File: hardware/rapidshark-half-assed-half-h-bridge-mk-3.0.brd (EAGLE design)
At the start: 25.4 x 40.6 mm, 31 parts, among them Q2 IRF540N

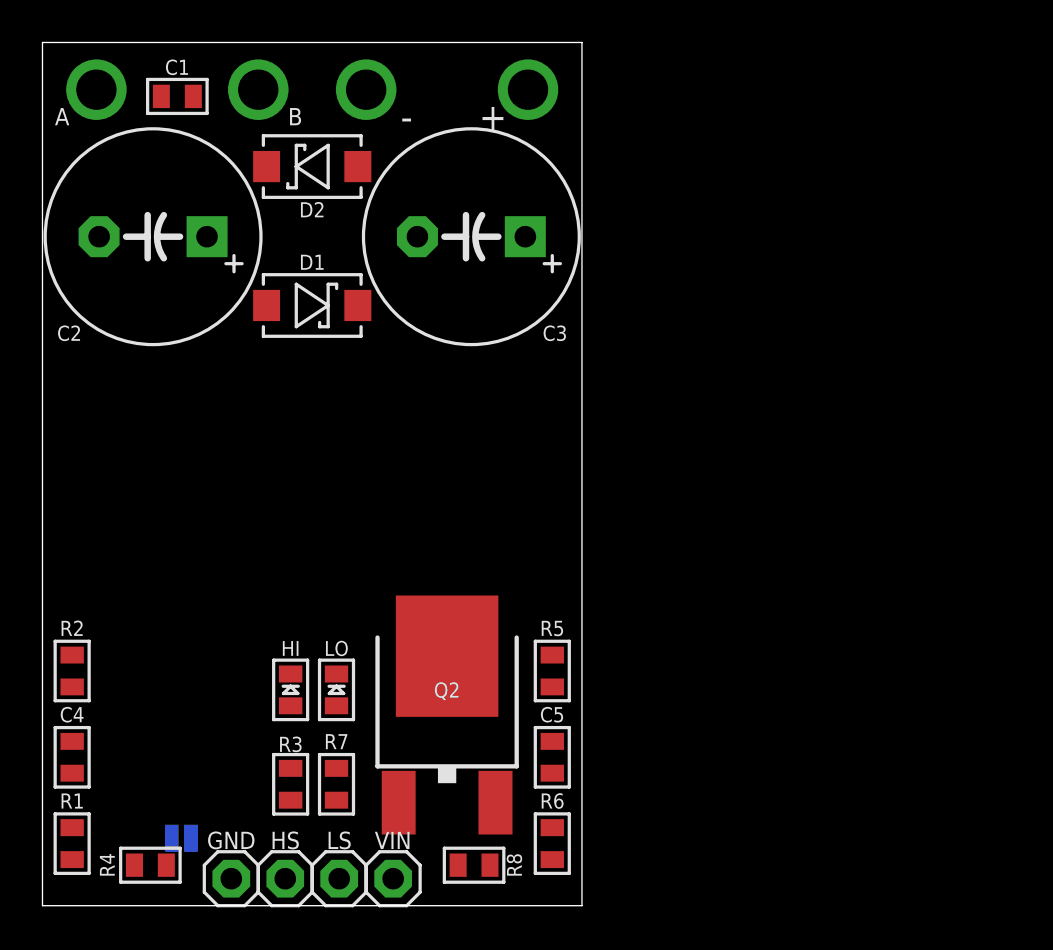
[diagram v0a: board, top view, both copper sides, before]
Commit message: WIP A3946 half bridge driver
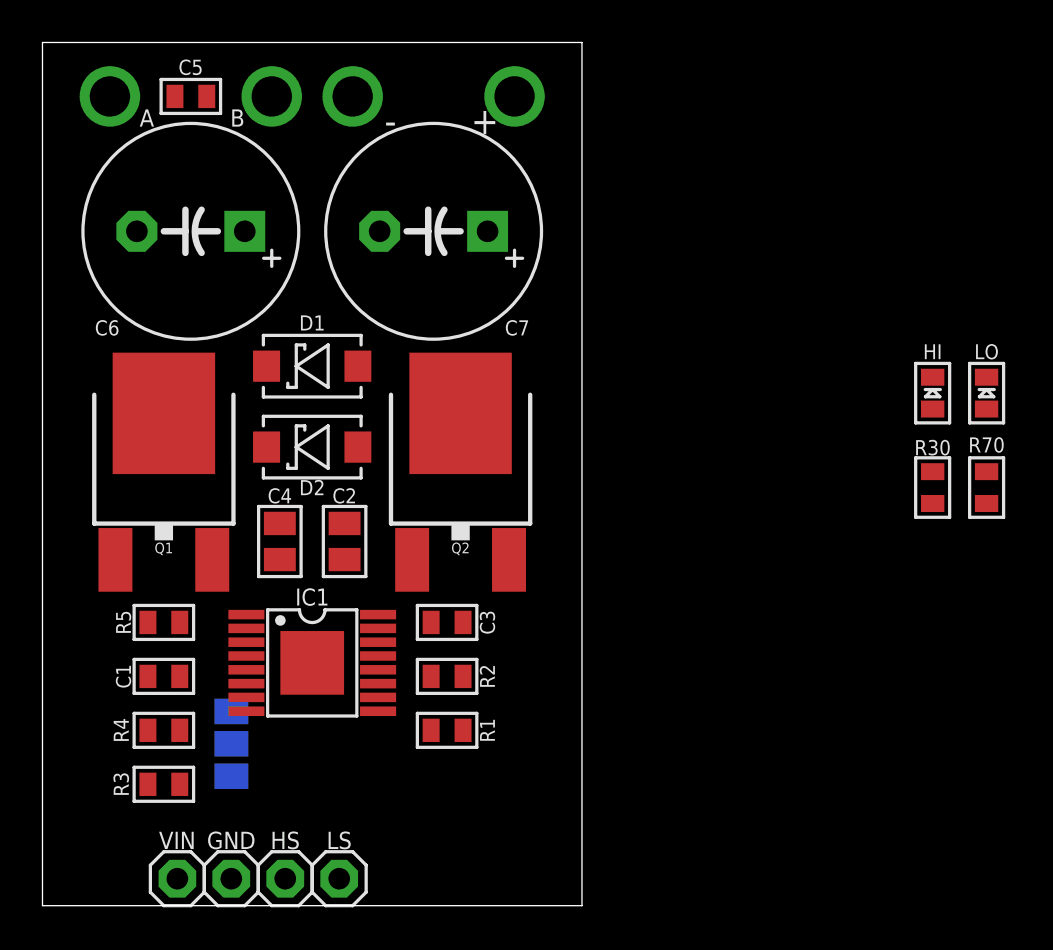
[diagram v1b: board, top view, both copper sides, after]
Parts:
- removed R6: 27R, a_parts:R0603-TIGHTER
- removed R7, R8: 330R, a_parts:R0603-TIGHTER
- removed SJ1: JUMPER-PAD-2-NO, a_parts:PAD-JUMPER-2-NO_NO_SILK
- added C6, C7: 470uF, a_parts:E5-10,5
- added IC1: A3946LP, a_parts:TSSOP-16-PAD
- added JP1: (no value), a_parts:PAD-JUMPER-3-NO_YES_SILK_FULL_BOX
- added Q1: IRLR3410, a_parts:DPAK
- added R30, R70: 330R, a_parts:R0603-TIGHTER
- C1: value 1uF -> 0.47uF
- C2: value 470uF -> 10uF; device a_parts:E5-10,5 -> a_parts:C0805-TIGHTER
- C3: value 470uF -> 0.1uF; device a_parts:E5-10,5 -> a_parts:C0603-TIGHTER
- C4: value 0.1uF -> 10uF; device a_parts:C0603-TIGHTER -> a_parts:C0805-TIGHTER
- C5: value 0.1uF -> 1uF
- Q2: value IRF540N -> IRLR3410
- R1: value 10k -> 10K
- R2: value 27R -> 15.8K
- R3, R4: value 330R -> 33R
- R5: value 10k -> 470K
- moved C5 35.5 mm to (6.99, 38.1), turned to 0 degrees
- moved LO 33.6 mm to (44.5, 24.1)
- moved HI 33.3 mm to (41.9, 24.1)
- moved C1 27.3 mm to (5.71, 10.8)
- moved R1 18.4 mm to (19.1, 8.26), turned to 0 degrees
- moved R5 18.4 mm to (5.71, 13.3), turned to 180 degrees
- moved C3 18.2 mm to (19.1, 13.3), turned to 0 degrees
- moved R2 17.7 mm to (19.1, 10.8), turned to 180 degrees
- moved C2 16.9 mm to (14.2, 17.1), turned to 90 degrees
- moved C4 14.1 mm to (11.2, 17.1)
- moved D2 13.2 mm to (12.7, 21.6)
- moved Q2 11.4 mm to (19.7, 21.6)
- moved VIN 10.2 mm to (6.35, 1.27)
- moved R4 6.38 mm to (5.71, 8.26)
- moved R3 5.97 mm to (5.71, 5.71), turned to 180 degrees
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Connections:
- removed net HS: HS.1, R3.1, R4.1
- removed net LS: LS.1, R7.1, R8.1
- new net !FAULT: IC1.9, R1.1
- new net IN1: IC1.10
- new net IN2: IC1.11
- new net N$11: IC1.5, R4.1
- new net N$12: IC1.7, R3.1
- new net RST: IC1.12
- new net VREF: C3.1, IC1.15, R1.2
- new net VREG: C4.1, IC1.1
- net A: now also C5.1, IC1.6, Q1.3, R5.1; no longer C1.1
- net GND: now also C3.2, C4.2, IC1.13, JP1.3, R2.1; no longer SJ1.1
- net N$1: now also R4.2; no longer R5.2, R6.2
- net N$2: now also C1.1, IC1.3; no longer R2.1
- net N$3: now also R70.2; no longer R7.2
- net N$4: now also R30.2; no longer R3.2
- net N$5: now also Q1.1, R3.2, R5.2; no longer R1.1, R2.2
- net N$6: now also C1.2, IC1.2; no longer R4.2
- net N$7: now also IC1.14, R2.2; no longer R8.2
- net N$8: now also IC1.PAD, JP1.2; no longer R6.1
- net PGND: now also C2.2, C6.-, C7.-, IC1.4, JP1.1; no longer C1.2, C2.-, C3.-, C4.2, R5.1, SJ1.2
- net VBAT: now also C2.1, C6.+, C7.+, IC1.16, Q1.4; no longer C2.+, C3.+, C4.1, C5.1, R1.2
